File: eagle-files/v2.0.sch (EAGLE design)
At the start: 35 parts, among them U2 MLX90614_

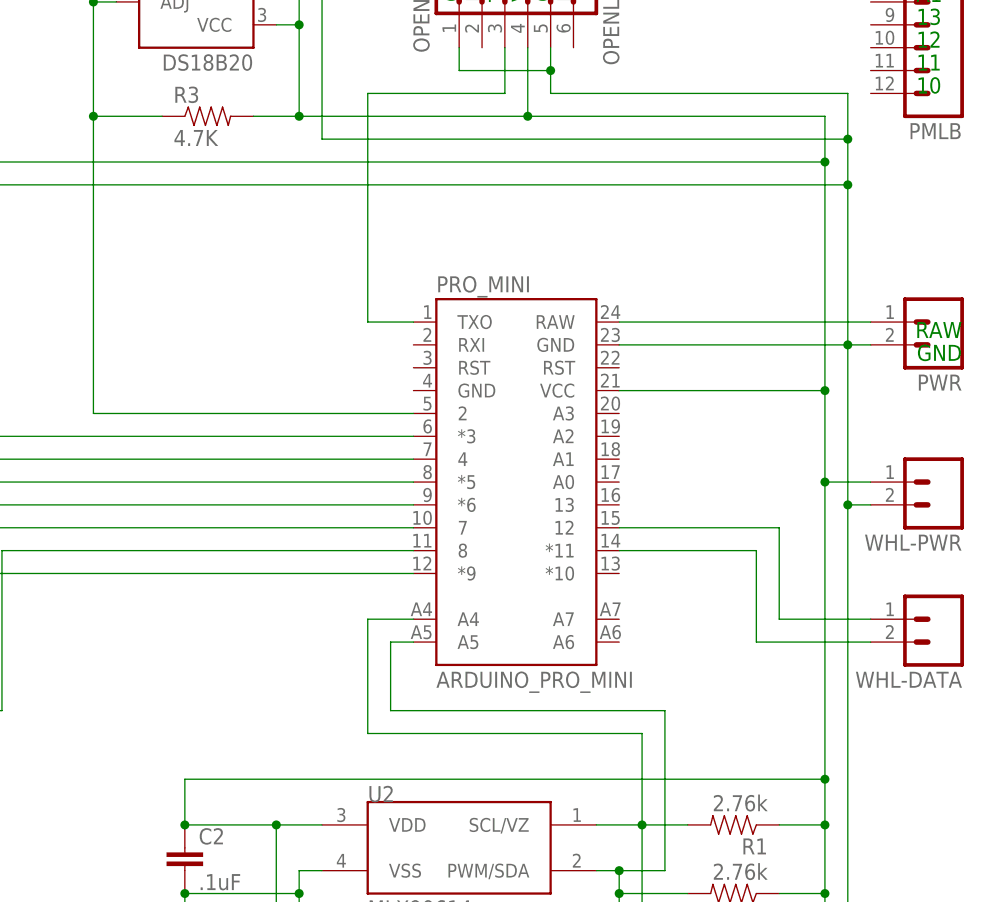
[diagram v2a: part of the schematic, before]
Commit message: added reset switch and flipped board
Moved parts around to make more room. I added a reset button, but I am
not sure it is wired correctly, I need to test it on an Uno to make
sure that I am not crazy.
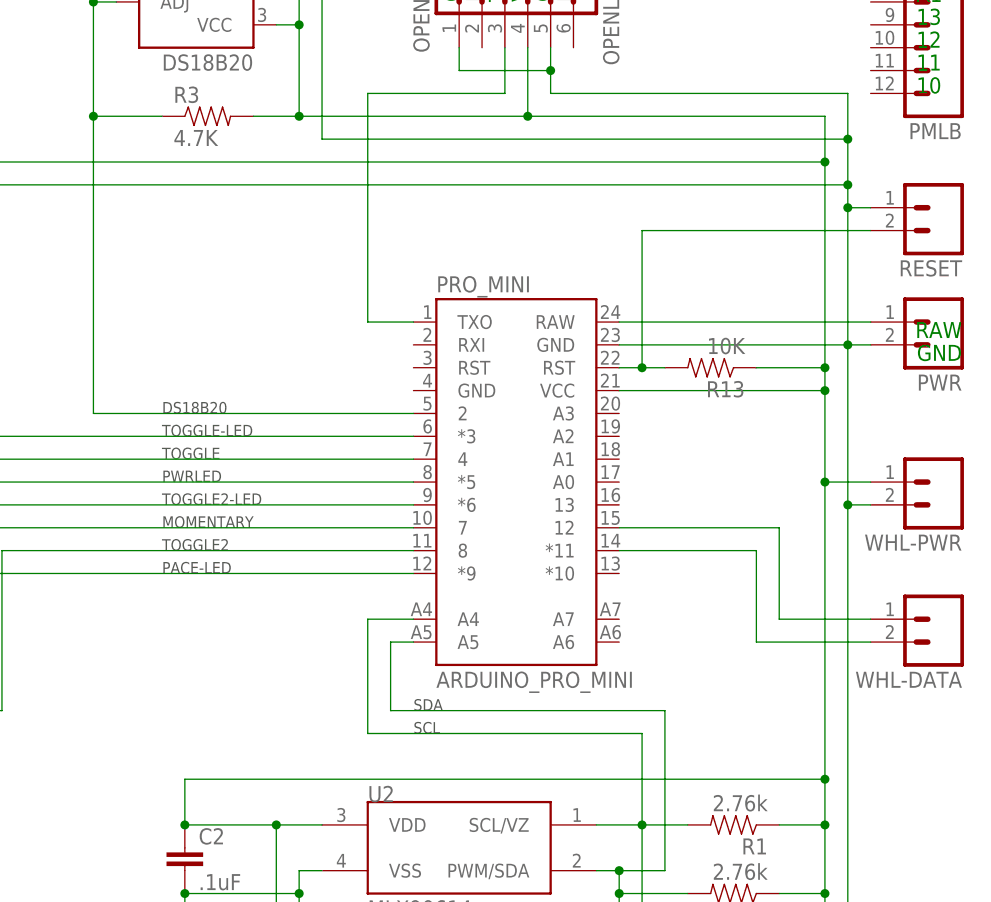
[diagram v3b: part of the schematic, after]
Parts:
- added R13: 10K, SparkFun-Resistors:10KOHM1/10W1%(0603)0603
- added RESET: M023.5MM_LOCK, SparkFun-Connectors:M023.5MM_LOCK
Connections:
- new net N$19: PRO_MINI.RST@2, R13.2, RESET.2
- net 5V: now also R13.1
- net GND: now also RESET.1
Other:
- note added: "DS18B20"
- note added: "MOMENTARY"
- note added: "PACE-LED"
- note added: "PWRLED"
- note added: "SCL"
- note added: "SDA"
- note added: "TOGGLE"
- note added: "TOGGLE-LED"
- note added: "TOGGLE2"
- note added: "TOGGLE2-LED"
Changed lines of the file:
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@@
 <class number="0" name="default" width="0" drill="0">
+</class>
+<class number="1" name="5V" width="0.6096" drill="0">
+</class>
+<class number="2" name="GND" width="0.6096" drill="0">
 </class>
 </classes>
@@
 <part name="R8" library="SparkFun-Resistors" deviceset="330OHM1/10W1%(0603)" device="" value="330"/>
 <part name="DS18B20-CON" library="SparkFun-Connectors" deviceset="M03" device="SCREW_LOCK" value="CON"/>
+<part name="RESET" library="SparkFun-Connectors" deviceset="M02" device="3.5MM_LOCK" value=""/>
+<part name="R13" library="SparkFun-Resistors" deviceset="10KOHM1/10W1%(0603)" device="0603" value="10K"/>
 </parts>
 <sheets>
@@
 MOMENTARY: Place mark
 TOGGEL2: time/distance data collection method</text>
+<text x="157.48" y="109.22" size="1.27" layer="97">TOGGLE</text>
+<text x="157.48" y="99.06" size="1.27" layer="97">TOGGLE2</text>
+<text x="157.48" y="101.6" size="1.27" layer="97">MOMENTARY</text>
+<text x="157.48" y="96.52" size="1.27" layer="97">PACE-LED</text>
+<text x="157.48" y="104.14" size="1.27" layer="97">TOGGLE2-LED</text>
+<text x="157.48" y="106.68" size="1.27" layer="97">PWRLED</text>
+<text x="157.48" y="111.76" size="1.27" layer="97">TOGGLE-LED</text>
+<text x="157.48" y="114.3" size="1.27" layer="97">DS18B20</text>
+<text x="185.42" y="81.28" size="1.27" layer="97">SDA</text>
+<text x="185.42" y="78.74" size="1.27" layer="97">SCL</text>
 </plain>
 <instances>
@@
 <instance part="R8" gate="G$1" x="83.82" y="147.32" rot="R90"/>
 <instance part="DS18B20-CON" gate="G$1" x="160.02" y="180.34" rot="R270"/>
+<instance part="RESET" gate="G$1" x="243.84" y="137.16" rot="R180"/>
+<instance part="R13" gate="G$1" x="218.44" y="119.38" rot="R180"/>
 </instances>
 <busses>
 </busses>
 <nets>
-<net name="GND" class="0">
+<net name="GND" class="2">
 <segment>
 <pinref part="OPENLOG1" gate="G$1" pin="1"/>
@@
 <wire x1="236.22" y1="121.92" x2="233.68" y2="121.92" width="0.1524" layer="91"/>
 <wire x1="233.68" y1="121.92" x2="208.28" y2="121.92" width="0.1524" layer="91"/>
+<junction x="233.68" y="121.92"/>
 <wire x1="233.68" y1="121.92" x2="233.68" y2="104.14" width="0.1524" layer="91"/>
-<junction x="233.68" y="121.92"/>
 <wire x1="233.68" y1="104.14" x2="233.68" y2="55.88" width="0.1524" layer="91"/>
 <wire x1="233.68" y1="55.88" x2="233.68" y2="40.64" width="0.1524" layer="91"/>
@@
 <pinref part="MLX1" gate="G$1" pin="4"/>
 <wire x1="233.68" y1="144.78" x2="233.68" y2="139.7" width="0.1524" layer="91"/>
-<wire x1="233.68" y1="139.7" x2="233.68" y2="121.92" width="0.1524" layer="91"/>
+<wire x1="233.68" y1="139.7" x2="233.68" y2="137.16" width="0.1524" layer="91"/>
+<wire x1="233.68" y1="137.16" x2="233.68" y2="121.92" width="0.1524" layer="91"/>
 <wire x1="187.96" y1="48.26" x2="187.96" y2="50.8" width="0.1524" layer="91"/>
 <wire x1="187.96" y1="50.8" x2="172.72" y2="50.8" width="0.1524" layer="91"/>
@@
 <wire x1="157.48" y1="167.64" x2="157.48" y2="172.72" width="0.1524" layer="91"/>
 <junction x="175.26" y="162.56"/>
+<pinref part="RESET" gate="G$1" pin="1"/>
+<wire x1="236.22" y1="137.16" x2="233.68" y2="137.16" width="0.1524" layer="91"/>
+<junction x="233.68" y="137.16"/>
 </segment>
 </net>
@@
 </segment>
 </net>
-<net name="5V" class="0">
+<net name="5V" class="1">
 <segment>
 <pinref part="PRO_MINI" gate="G$1" pin="VCC"/>
@@
 <junction x="231.14" y="116.84"/>
 <pinref part="R2" gate="G$1" pin="1"/>
-<wire x1="231.14" y1="142.24" x2="231.14" y2="116.84" width="0.1524" layer="91"/>
+<wire x1="231.14" y1="142.24" x2="231.14" y2="119.38" width="0.1524" layer="91"/>
+<wire x1="231.14" y1="119.38" x2="231.14" y2="116.84" width="0.1524" layer="91"/>
 <wire x1="226.06" y1="60.96" x2="231.14" y2="60.96" width="0.1524" layer="91"/>
 <pinref part="R1" gate="G$1" pin="1"/>
@@
 <wire x1="162.56" y1="170.18" x2="162.56" y2="172.72" width="0.1524" layer="91"/>
 <junction x="172.72" y="157.48"/>
+<pinref part="R13" gate="G$1" pin="1"/>
+<wire x1="223.52" y1="119.38" x2="231.14" y2="119.38" width="0.1524" layer="91"/>
+<junction x="231.14" y="119.38"/>
 </segment>
 </net>
@@
 </segment>
 </net>
+<net name="N$19" class="0">
+<segment>
+<pinref part="PRO_MINI" gate="G$1" pin="RST@2"/>
+<pinref part="R13" gate="G$1" pin="2"/>
+<wire x1="213.36" y1="119.38" x2="210.82" y2="119.38" width="0.1524" layer="91"/>
+<pinref part="RESET" gate="G$1" pin="2"/>
+<wire x1="210.82" y1="119.38" x2="208.28" y2="119.38" width="0.1524" layer="91"/>
+<wire x1="236.22" y1="134.62" x2="210.82" y2="134.62" width="0.1524" layer="91"/>
+<wire x1="210.82" y1="134.62" x2="210.82" y2="119.38" width="0.1524" layer="91"/>
+<junction x="210.82" y="119.38"/>
+</segment>
+</net>

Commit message: Added an analog hookup.
Moved a few things, but not much.
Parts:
- removed PMLB: Side, SparkFun:M12PTH
- added A0: (no value), SparkFun-Connectors:M03SCREW_LOCK
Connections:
- new net N$20: A0.3, PRO_MINI.A0
- net 5V: now also A0.1
- net GND: now also A0.2
- net N$11: now also PRO_MINI.*10; no longer PRO_MINI.*11
- net N$3: now also PRO_MINI.*11; no longer PRO_MINI.12
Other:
- note removed: "10"
- note removed: "11"
- note removed: "12"
- note removed: "13"
- note removed: "A1"
- note removed: "A2"
- note removed: "A3"
- moved on the sheet: C2, DS18B20, DS18B20-CON, MLX1, MOMENTARY, OPENLOG1, PACE-LED, PRO_MINI, PWR, PWRLED, R1, R10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
